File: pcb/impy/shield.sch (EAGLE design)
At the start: 118 parts, among them J1 USB-2410-06, J2 SI-60062-F, J3 5V, U1 AD5933YRS, U10 LTC3406AB, U11 23LCV1024-I/SN, U12 MIC2009A-1YM6, U13 ADG725BSU, U14 ADG725BSU, U2 ADG704BRM, U3 AD8656ARZ, U4 M24C08WMN, U5 ADG706BRU, U6 DP83848I, U7 MIC2009A-1YM6, U8 AT25DF081A-SS, U9 SST25VF080B-80-4I-S2

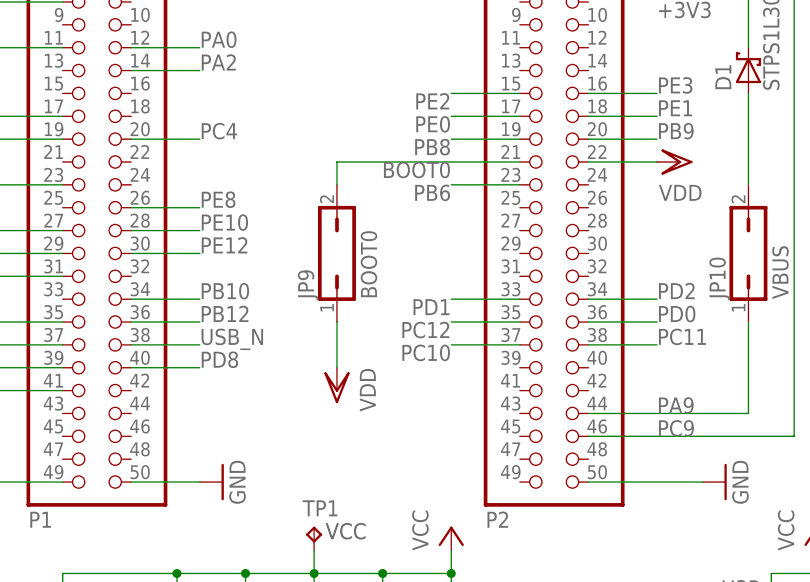
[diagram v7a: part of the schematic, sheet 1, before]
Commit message: * pcb/impy: (shield.sch) Remove unnecessary BOOT0 jumper, this can be accessed on the discovery board directly.
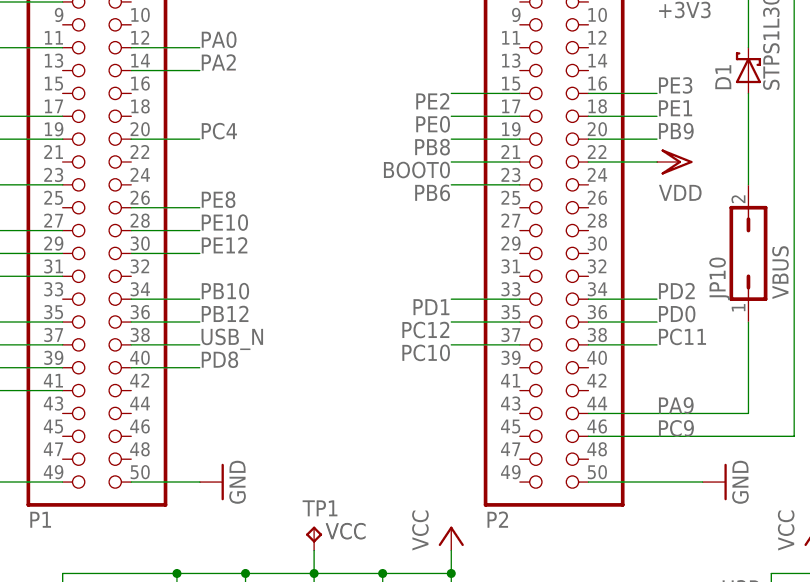
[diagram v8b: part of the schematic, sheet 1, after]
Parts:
- removed JP9: BOOT0, jumper:JP1Q
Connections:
- net BOOT0: no longer JP9.2
- net VDD: no longer JP9.1
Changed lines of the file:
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@@
 <part name="P+30" library="supply1" deviceset="VCC" device=""/>
 <part name="SJ2" library="jumper" deviceset="SJ" device="" value="ETH_CLK"/>
-<part name="JP9" library="jumper" deviceset="JP1Q" device="" value="BOOT0"/>
-<part name="VDD5" library="supply1" deviceset="VDD" device=""/>
 <part name="S2" library="parts" deviceset="FSM4JSMATR" device=""/>
 <part name="S1" library="parts" deviceset="FSM4JSMATR" device=""/>
@@
 <instance part="C22" gate="G$1" x="63.5" y="5.08"/>
 <instance part="SJ2" gate="1" x="48.26" y="88.9"/>
-<instance part="JP9" gate="A" x="50.8" y="45.72"/>
-<instance part="VDD5" gate="G$1" x="50.8" y="30.48" rot="R180"/>
 <instance part="S2" gate="G$1" x="190.5" y="58.42"/>
 <instance part="S1" gate="G$1" x="190.5" y="73.66"/>
@@
 <pinref part="JP2" gate="A" pin="22"/>
 <wire x1="86.36" y1="55.88" x2="78.74" y2="55.88" width="0.1524" layer="91"/>
-</segment>
-<segment>
-<pinref part="JP9" gate="A" pin="1"/>
-<wire x1="50.8" y1="33.02" x2="50.8" y2="38.1" width="0.1524" layer="91"/>
-<pinref part="VDD5" gate="G$1" pin="VDD"/>
 </segment>
 <segment>
@@
 <pinref part="JP2" gate="A" pin="21"/>
 <label x="63.5" y="55.88" size="1.778" layer="95" rot="R180"/>
-<pinref part="JP9" gate="A" pin="2"/>
-<wire x1="50.8" y1="53.34" x2="50.8" y2="55.88" width="0.1524" layer="91"/>
-<wire x1="50.8" y1="55.88" x2="71.12" y2="55.88" width="0.1524" layer="91"/>
+<wire x1="63.5" y1="55.88" x2="71.12" y2="55.88" width="0.1524" layer="91"/>
 </segment>
 </net>
